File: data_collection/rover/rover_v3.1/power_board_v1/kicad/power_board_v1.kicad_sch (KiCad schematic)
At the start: 133 parts, among them J1 XT60_BATT, J10 from Pi USB2, J11 UPDI prog (UPDI/3V3/GND), J12 5V_A pigtail hdr DNP, J13 USB_A port3 (3A), J14 from Pi USB3, J2 PANEL_SW, J3 USB4105-GF-A (TH shell), J4 USB_A radio1, J5 USB_A radio2, J6 AUX 5V 2A, J7 PI GPIO harness, J8 AUX_CTL out (JST-GH), J9 from Pi USB1, Q2 CSD18543Q3A diode, Q3 CSD18543Q3A switch, U1 LM5145 rail A, U10 TPS2557 ~3A (always on), U2 LM5145 rail B, U3 ATtiny816 (SOIC-20), U4 LM74800-Q1, U5 INA226 (addr 0x40), U6 TPS7A1633 3V3 60V LDO, U7 TPS2557 ~3A, U8 TPS2557 ~3A, U9 AP2112K-3.3 (switched)

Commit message: power_board v4.5: sync U3 value to ATtiny1616-SN across generator/sch/netlist/board/BOM/CPL
Closes the drift from the LCSC-only substitution (33571a4): U3's value now
reads 'ATtiny1616-SN (816-compat)' everywhere — schematic PDF, assembly
docs, and BOM Comment agree with the part JLC actually places (C614136).
Also retires the never-orderable 'ATtiny816-SSN' string. DRC/parity
re-verified: 0/0/0. Submission zip rebuilt.

Co-Authored-By: Claude Fable 5 <noreply@anthropic.com>
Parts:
- U3: value ATtiny816 (SOIC-20) -> ATtiny1616-SN (816-compat)

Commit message: power_board v4.7: D5 (rev-batt schottky) and D4 (LED) were REVERSED — polarity convention fix
KiCad footprint convention: pad 1 = cathode (verified from the footprints'
own marker graphics). D5 had pin1=VBATT_F -> cathode on the battery side,
blocking the always-on LDO: the supervisor MCU could never power. D4's LED
was reversed. Both invisible to DRC/audit/parity (electrically
self-consistent). Caught during the JLC order polarity audit.

- generator: LED symbol pin1 renamed K, D5/D4 net maps swapped so pin1
  carries the cathode net; structure links updated
- board: D5/D4 rotated 180 with pad nets rebound (copper untouched);
  flipped ref texts relocated
- DRC 0/0, parity clean, audit PASS; fab + submission zip rebuilt
- docs/learnings.md: the bug class and the standing pad1-cathode rule

Co-Authored-By: Claude Fable 5 <noreply@anthropic.com>
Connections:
- net GND: now also D4.1 (K); no longer D4.2 (K)
- net LED_K: now also D4.2 (A); no longer D4.1 (A)
- net VBATT_F: now also D5.2; no longer D5.1
- net VBATT_FD: now also D5.1; no longer D5.2

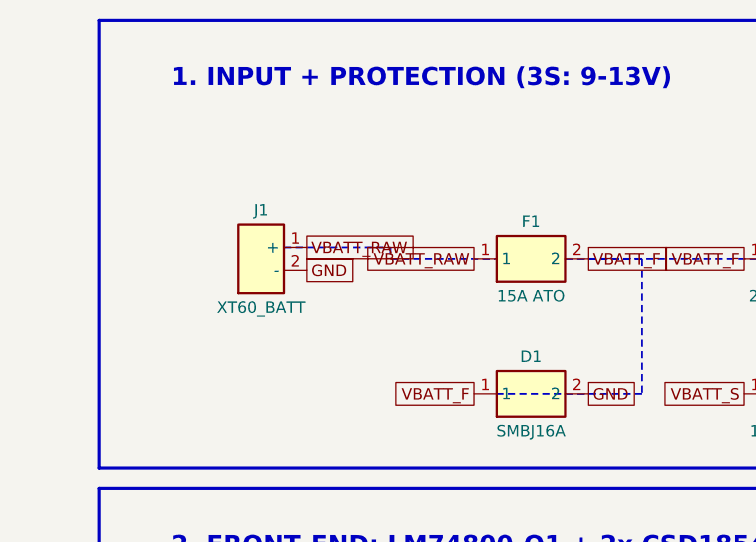
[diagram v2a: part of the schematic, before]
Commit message: power_board v4.8: XT60 battery polarity was REVERSED — + net was on the '-' blade
KiCad's AMASS_XT60PW-M pad 1 is the '-' blade (footprint's own silk +
JLC/EasyEDA data agree). Symbol pin1='+' put VBATT_RAW on it: correctly
wired batteries would present reverse polarity — FE blocks, board DOA.
Third symbol-vs-footprint polarity bug today (after D5/D4).

- symbol pins renamed (1='-', 2='+'), J1 net map swapped, links updated
- board: J1 pad nets swapped; old VBATT_RAW/GND runs ripped; new 1.2mm
  VBATT_RAW run to the north blade -> F1; GND blade via pours/plane
- rotation DB: AMASS_XT60PW-M +270 (board now matches JLC model zero)
- DRC 0/0, parity clean, audit PASS; fab + submission zip rebuilt

Co-Authored-By: Claude Fable 5 <noreply@anthropic.com>
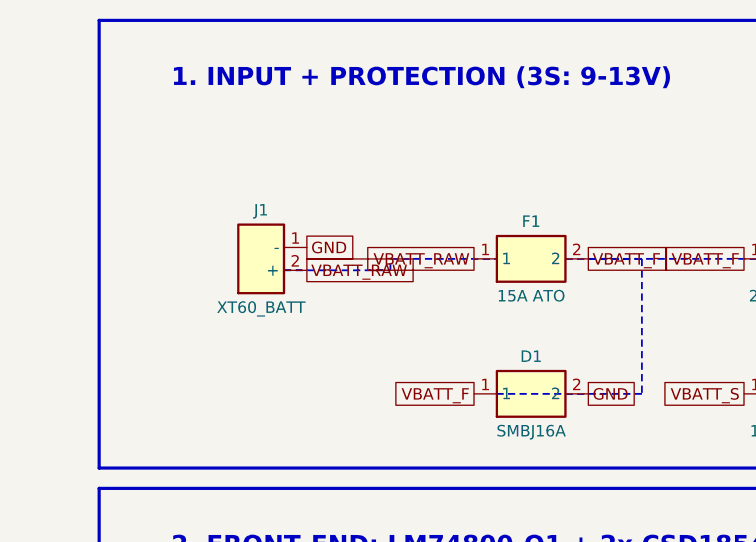
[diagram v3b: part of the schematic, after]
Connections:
- net GND: now also J1.1 (-); no longer J1.2 (-)
- net VBATT_RAW: now also J1.2 (+); no longer J1.1 (+)
